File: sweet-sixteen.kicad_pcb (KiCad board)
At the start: 2 copper layers, 113 x 105.4 mm, 87 parts, among them P1 SDA_I, P10 VIN_O, P11 GND_O, P12 SDA_O, P13 CLK_O, P14 LE_O, P15 ~OE_O, P2 CLK_I, P3 LE_I, P4 ~OE_I, P5 CONN_02X20, P6 5V_I, P7 VIN_I, P8 GND_I, P9 5V_O, U1 OKI-T/3-W40, U10 STP16CPC26, U11 STP16CPC26, U12 STP16CPC26, U13 74HCT08, U2 STP16CPC26, U3 OKI-T/3-W40, U4 STP16CPC26, U5 74HCT08, U6 STP16CPC26, U7 STP16CPC26, U8 STP16CPC26, U9 STP16CPC26

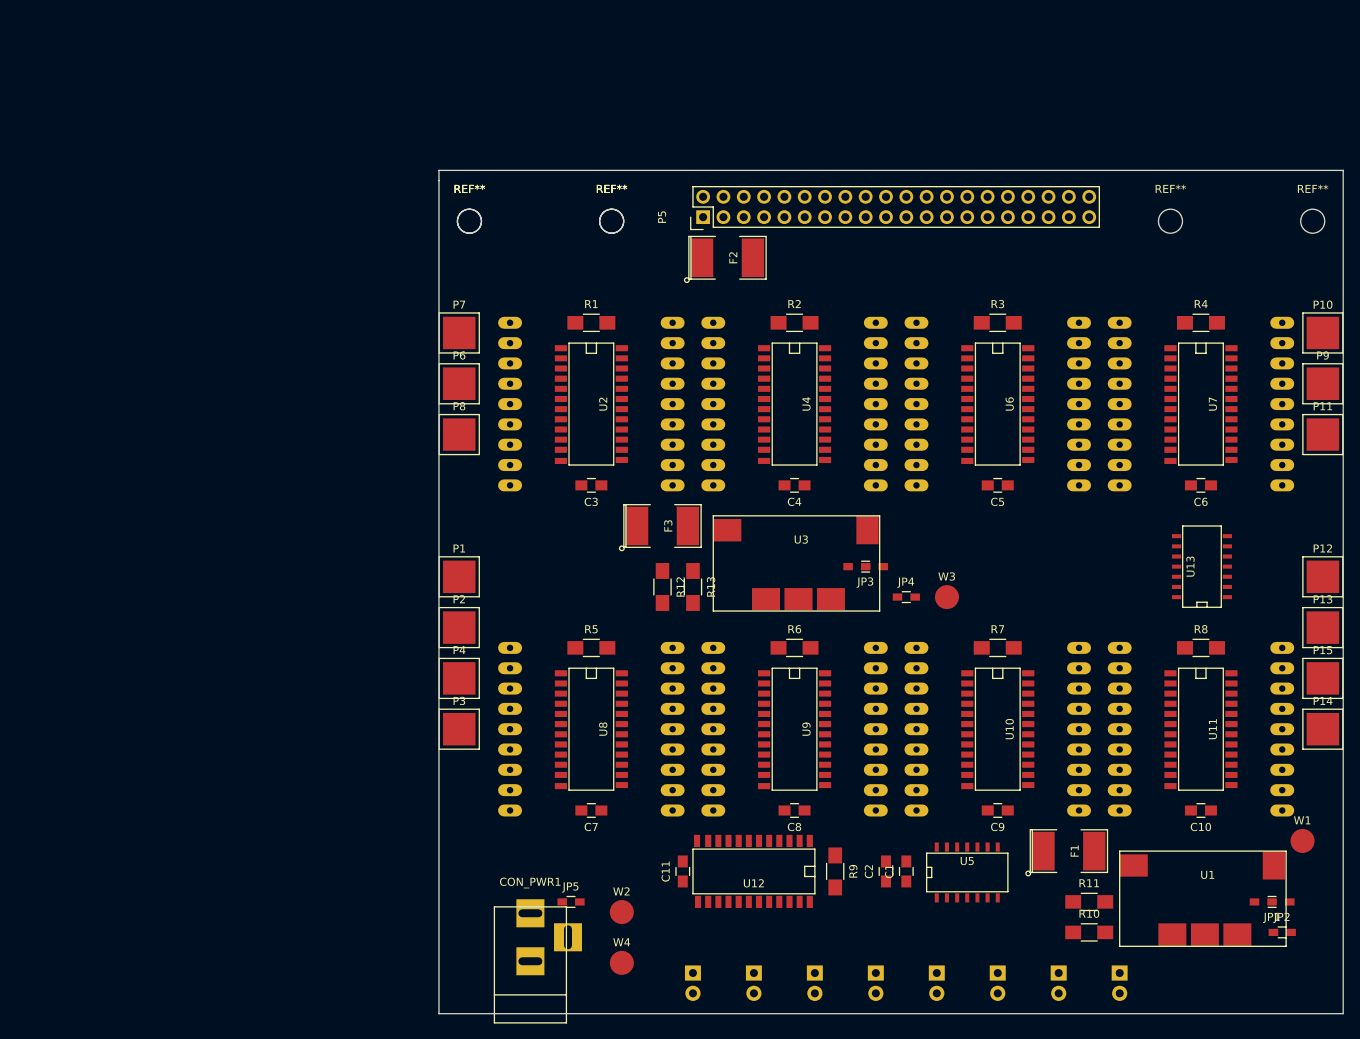
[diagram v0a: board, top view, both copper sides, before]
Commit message: (remove) mounting hole text, move mounting holes
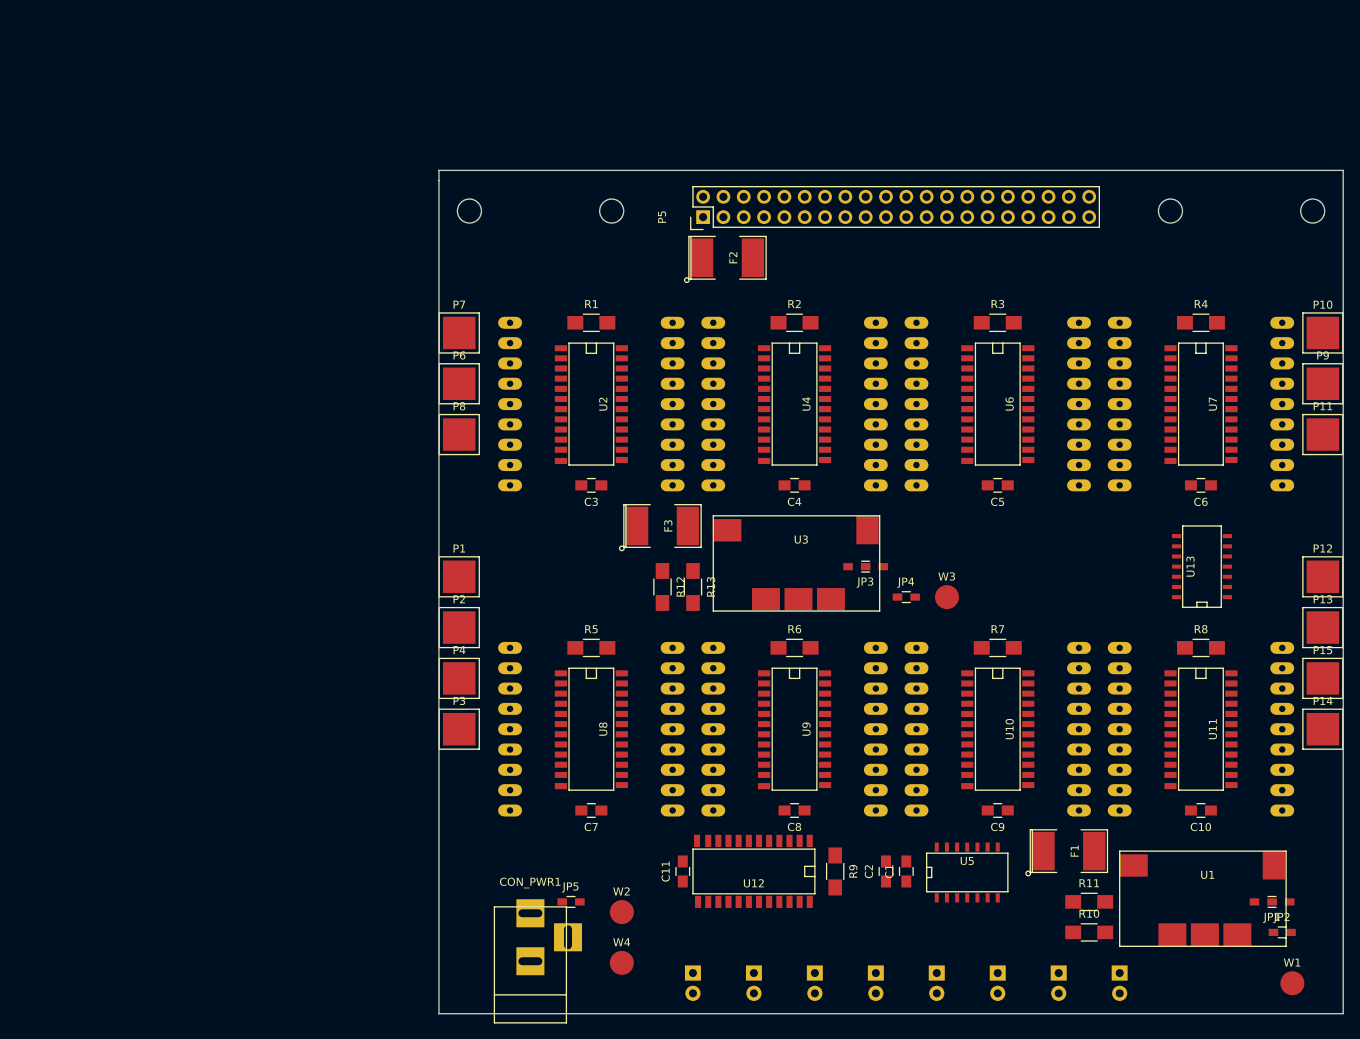
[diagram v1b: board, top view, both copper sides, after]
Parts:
- removed REF** (x2): MountingHole_3mm, Mounting_Holes:MountingHole_3mm
- moved W1 17.8 mm to (196.8, 133.3)
- moved ? 1.27 mm to (94.0, 36.8)
- moved ? 1.27 mm to (111.8, 36.8)
- moved ? 1.27 mm to (199.4, 36.8)
- moved ? 1.27 mm to (181.6, 36.8)
- renumbered REF** to ?
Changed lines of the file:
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@@
     (links 326)
     (no_connects 326)
-    (area 90.094999 31.674999 203.275001 137.235001)
+    (area 87.491474 31.674999 207.880046 138.585621)
     (thickness 1.6)
     (drawings 5)
     (tracks 0)
     (zones 0)
-    (modules 87)
+    (modules 85)
     (nets 191)
   )
@@
   )
   (module Mounting_Holes:MountingHole_3mm (layer F.Cu)
-    (at 93.98 38.1)
+    (at 93.98 36.83)
     (descr "Mounting hole, Befestigungsbohrung, 3mm, No Annular, Kein Restring,")
     (tags "Mounting hole, Befestigungsbohrung, 3mm, No Annular, Kein Restring,")
-    (fp_text reference REF** (at 0 -4.0005) (layer F.SilkS)
-      (effects (font (size 1 1) (thickness 0.15)))
-    )
-    (fp_text value MountingHole_3mm (at 1.00076 5.00126) (layer F.Fab)
+    (fp_text reference "" (at 0 0) (layer F.SilkS)
+      (effects (font (size 1 1) (thickness 0.15)))
+    )
+    (fp_text value MountingHole_3mm (at -12.7 -3.81) (layer F.Fab)
       (effects (font (size 1 1) (thickness 0.15)))
     )
@@
   )
   (module Mounting_Holes:MountingHole_3mm (layer F.Cu)
-    (at 111.76 38.1)
+    (at 111.76 36.83)
     (descr "Mounting hole, Befestigungsbohrung, 3mm, No Annular, Kein Restring,")
     (tags "Mounting hole, Befestigungsbohrung, 3mm, No Annular, Kein Restring,")
-    (fp_text reference REF** (at 0 -4.0005) (layer F.SilkS)
-      (effects (font (size 1 1) (thickness 0.15)))
-    )
-    (fp_text value MountingHole_3mm (at 1.00076 5.00126) (layer F.Fab)
-      (effects (font (size 1 1) (thickness 0.15)))
-    )
-    (fp_circle (center 0 0) (end 3 0) (layer Cmts.User) (width 0.381))
-    (pad 1 thru_hole circle (at 0 0) (size 3 3) (drill 3) (layers))
-  )
-  (module Mounting_Holes:MountingHole_3mm (layer F.Cu)
-    (at 111.76 38.1)
-    (descr "Mounting hole, Befestigungsbohrung, 3mm, No Annular, Kein Restring,")
-    (tags "Mounting hole, Befestigungsbohrung, 3mm, No Annular, Kein Restring,")
-    (fp_text reference REF** (at 0 -4.0005) (layer F.SilkS)
-      (effects (font (size 1 1) (thickness 0.15)))
-    )
-    (fp_text value MountingHole_3mm (at 1.00076 5.00126) (layer F.Fab)
+    (fp_text reference "" (at 0 0) (layer F.SilkS)
+      (effects (font (size 1 1) (thickness 0.15)))
+    )
+    (fp_text value MountingHole_3mm (at -30.48 -2.54) (layer F.Fab)
       (effects (font (size 1 1) (thickness 0.15)))
     )
@@
   )
   (module Measurement_Points:Measurement_Point_Round-SMD-Pad_Big (layer F.Cu)
-    (at 198.12 115.57)
+    (at 196.85 133.35)
     (descr "Mesurement Point, Round, SMD Pad, DM 3mm,")
     (tags "Mesurement Point, Round, SMD Pad, DM 3mm,")
@@
   )
   (module Mounting_Holes:MountingHole_3mm (layer F.Cu)
-    (at 93.98 38.1)
+    (at 199.39 36.83)
     (descr "Mounting hole, Befestigungsbohrung, 3mm, No Annular, Kein Restring,")
     (tags "Mounting hole, Befestigungsbohrung, 3mm, No Annular, Kein Restring,")
-    (fp_text reference REF** (at 0 -4.0005) (layer F.SilkS)
-      (effects (font (size 1 1) (thickness 0.15)))
-    )
-    (fp_text value MountingHole_3mm (at 1.00076 5.00126) (layer F.Fab)
+    (fp_text reference "" (at 0 0) (layer F.SilkS)
+      (effects (font (size 1 1) (thickness 0.15)))
+    )
+    (fp_text value MountingHole_3mm (at 12.7 -5.08) (layer F.Fab)
       (effects (font (size 1 1) (thickness 0.15)))
     )
@@
   )
   (module Mounting_Holes:MountingHole_3mm (layer F.Cu)
-    (at 199.39 38.1)
+    (at 181.61 36.83)
     (descr "Mounting hole, Befestigungsbohrung, 3mm, No Annular, Kein Restring,")
     (tags "Mounting hole, Befestigungsbohrung, 3mm, No Annular, Kein Restring,")
-    (fp_text reference REF** (at 0 -4.0005) (layer F.SilkS)
-      (effects (font (size 1 1) (thickness 0.15)))
-    )
-    (fp_text value MountingHole_3mm (at 1.00076 5.00126) (layer F.Fab)
-      (effects (font (size 1 1) (thickness 0.15)))
-    )
-    (fp_circle (center 0 0) (end 3 0) (layer Cmts.User) (width 0.381))
-    (pad 1 thru_hole circle (at 0 0) (size 3 3) (drill 3) (layers))
-  )
-  (module Mounting_Holes:MountingHole_3mm (layer F.Cu)
-    (at 181.61 38.1)
-    (descr "Mounting hole, Befestigungsbohrung, 3mm, No Annular, Kein Restring,")
-    (tags "Mounting hole, Befestigungsbohrung, 3mm, No Annular, Kein Restring,")
-    (fp_text reference REF** (at 0 -4.0005) (layer F.SilkS)
-      (effects (font (size 1 1) (thickness 0.15)))
-    )
-    (fp_text value MountingHole_3mm (at 1.00076 5.00126) (layer F.Fab)
-      (effects (font (size 1 1) (thickness 0.15)))
-    )
+    (fp_text reference "" (at 0 0) (layer F.SilkS)
+      (effects (font (size 1 1) (thickness 0.15)))
+    )
+    (fp_text value MountingHole_3mm (at 30.48 -3.81) (layer F.Fab)
+      (effects (font (size 1 1) (thickness 0.15)))
+    )

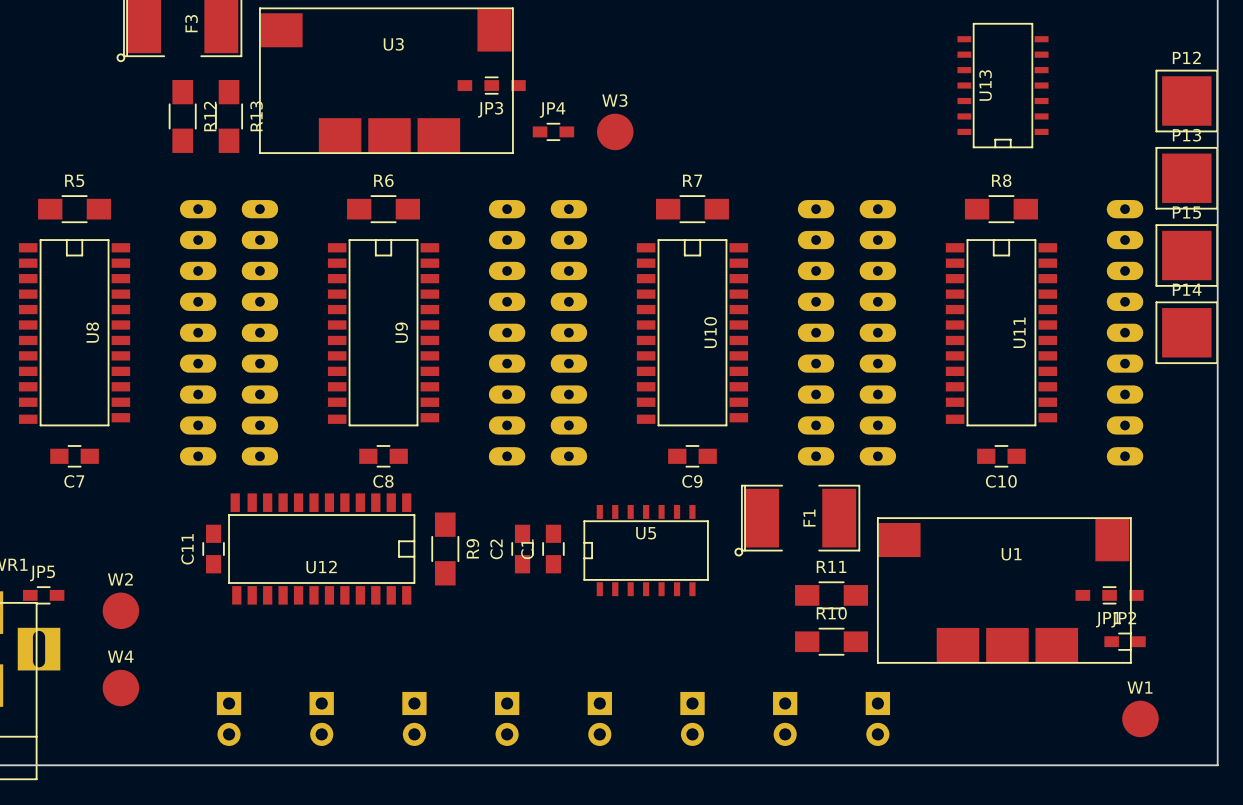
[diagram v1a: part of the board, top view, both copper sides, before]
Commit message: add more gnd-testpoints, move testpoint-labels to silkscreen
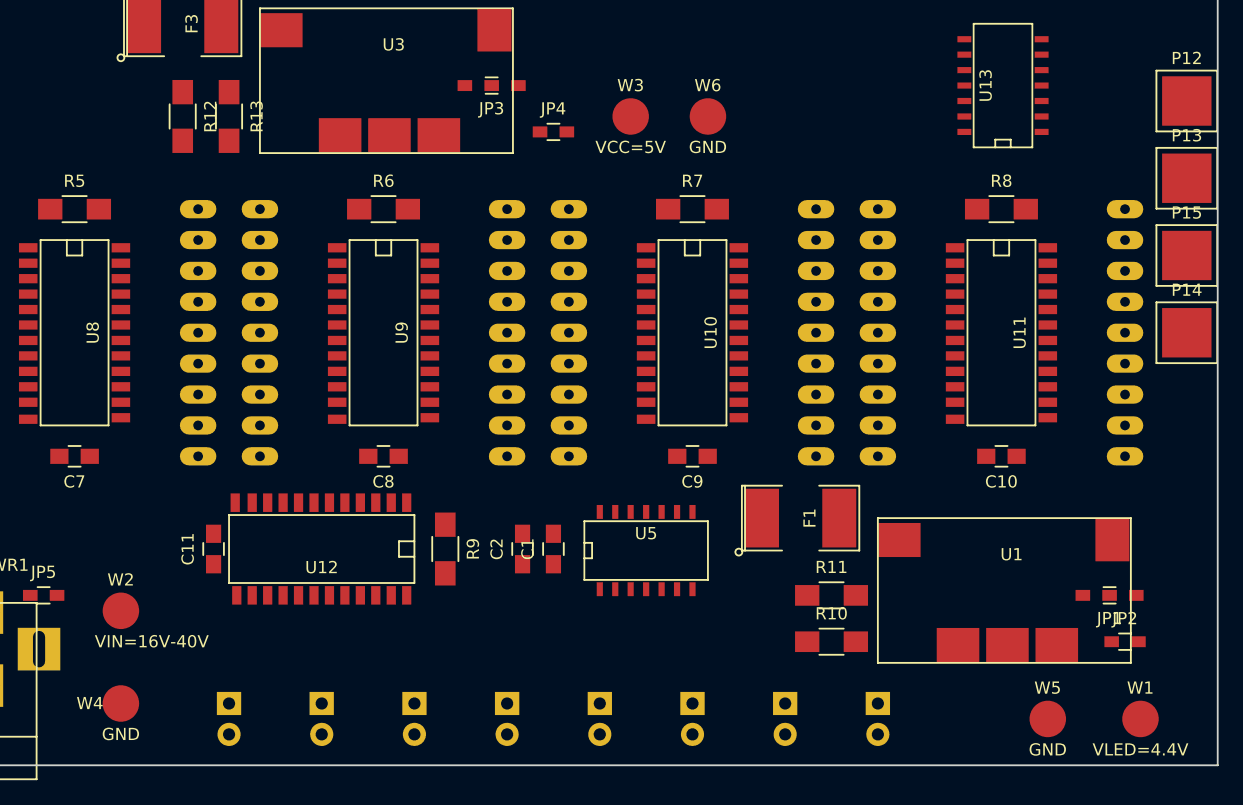
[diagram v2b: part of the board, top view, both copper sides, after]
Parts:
- added W5: GND, Measurement_Points:Measurement_Point_Round-SMD-Pad_Big, F.Cu at (189.2, 133.3)
- added W6: GND, Measurement_Points:Measurement_Point_Round-SMD-Pad_Big, F.Cu at (161.3, 83.8)
- moved W3 1.80 mm to (154.9, 83.8)
- moved W4 1.27 mm to (113.0, 132.1)
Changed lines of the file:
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@@
 (kicad_pcb (version 4) (host pcbnew 4.0.2+dfsg1-stable)
   (general
-    (links 326)
-    (no_connects 326)
-    (area 87.491474 31.674999 207.880046 138.585621)
+    (links 328)
+    (no_connects 328)
+    (area 90.094999 31.674999 203.275001 137.235001)
     (thickness 1.6)
     (drawings 5)
     (tracks 0)
     (zones 0)
-    (modules 85)
+    (modules 87)
     (nets 191)
   )
@@
       (effects (font (size 1 1) (thickness 0.15)))
     )
-    (fp_text value VLED=4.4V (at 2.54 3.81) (layer F.Fab)
+    (fp_text value VLED=4.4V (at 0 2.54) (layer F.SilkS)
       (effects (font (size 1 1) (thickness 0.15)))
     )
@@
       (effects (font (size 1 1) (thickness 0.15)))
     )
-    (fp_text value VIN=16V-40V (at 2.54 3.81) (layer F.Fab)
+    (fp_text value VIN=16V-40V (at 2.54 2.54) (layer F.SilkS)
       (effects (font (size 1 1) (thickness 0.15)))
     )
@@
   )
   (module Measurement_Points:Measurement_Point_Round-SMD-Pad_Big (layer F.Cu)
-    (at 153.67 85.09)
+    (at 154.94 83.82)
     (descr "Mesurement Point, Round, SMD Pad, DM 3mm,")
     (tags "Mesurement Point, Round, SMD Pad, DM 3mm,")
@@
       (effects (font (size 1 1) (thickness 0.15)))
     )
-    (fp_text value VCC=5V (at 2.54 3.81) (layer F.Fab)
+    (fp_text value VCC=5V (at 0 2.54) (layer F.SilkS)
       (effects (font (size 1 1) (thickness 0.15)))
     )
@@
   )
   (module Measurement_Points:Measurement_Point_Round-SMD-Pad_Big (layer F.Cu)
-    (at 113.03 130.81)
+    (at 113.03 132.08)
     (descr "Mesurement Point, Round, SMD Pad, DM 3mm,")
     (tags "Mesurement Point, Round, SMD Pad, DM 3mm,")
-    (fp_text reference W4 (at 0 -2.54) (layer F.SilkS)
+    (fp_text reference W4 (at -2.54 0) (layer F.SilkS)
       (effects (font (size 1 1) (thickness 0.15)))
     )
-    (fp_text value GND (at 2.54 3.81) (layer F.Fab)
+    (fp_text value GND (at 0 2.54) (layer F.SilkS)
       (effects (font (size 1 1) (thickness 0.15)))
     )
@@
       (net 15 /VLED))
   )
+  (module Measurement_Points:Measurement_Point_Round-SMD-Pad_Big (layer F.Cu)
+    (at 189.23 133.35)
+    (descr "Mesurement Point, Round, SMD Pad, DM 3mm,")
+    (tags "Mesurement Point, Round, SMD Pad, DM 3mm,")
+    (fp_text reference W5 (at 0 -2.54) (layer F.SilkS)
+      (effects (font (size 1 1) (thickness 0.15)))
+    )
+    (fp_text value GND (at 0 2.54) (layer F.SilkS)
+      (effects (font (size 1 1) (thickness 0.15)))
+    )
+    (pad 1 smd circle (at 0 0) (size 2.99974 2.99974) (layers F.Cu F.Paste F.Mask)
+      (net 139 GND))
+  )
+  (module Measurement_Points:Measurement_Point_Round-SMD-Pad_Big (layer F.Cu)
+    (at 161.29 83.82)
+    (descr "Mesurement Point, Round, SMD Pad, DM 3mm,")
+    (tags "Mesurement Point, Round, SMD Pad, DM 3mm,")
+    (fp_text reference W6 (at 0 -2.54) (layer F.SilkS)
+      (effects (font (size 1 1) (thickness 0.15)))
+    )
+    (fp_text value GND (at 0 2.54) (layer F.SilkS)
+      (effects (font (size 1 1) (thickness 0.15)))
+    )
+    (pad 1 smd circle (at 0 0) (size 2.99974 2.99974) (layers F.Cu F.Paste F.Mask)
+      (net 139 GND))
+  )
   (gr_line (start 90.17 33.02) (end 90.17 31.75) (angle 90) (layer Edge.Cuts) (width 0.15))
